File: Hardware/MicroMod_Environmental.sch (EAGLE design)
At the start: 36 parts, among them J1 MICROMOD_STANDARD, U1 SGP40, U2 EEPROM, U3 SHTC3, U4 3.3V, U5 STC31

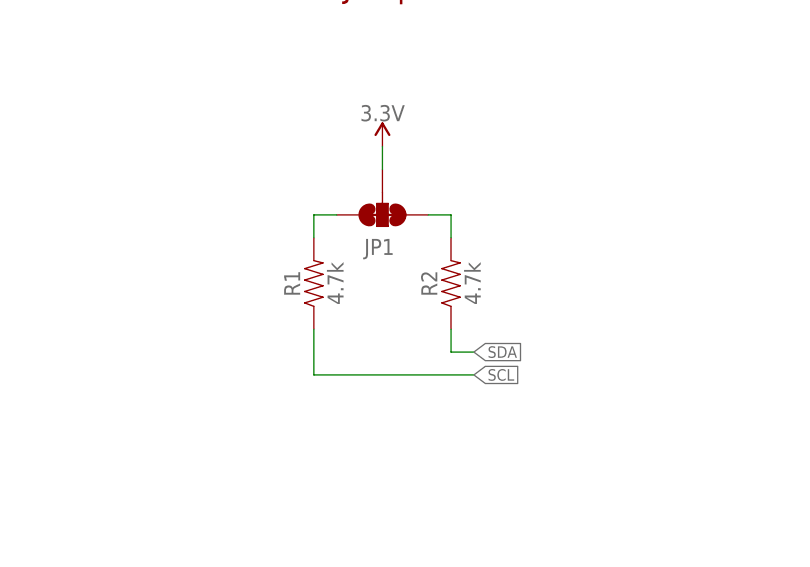
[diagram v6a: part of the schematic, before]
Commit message: Updates pull up resistors to 2.2k from 4.7k
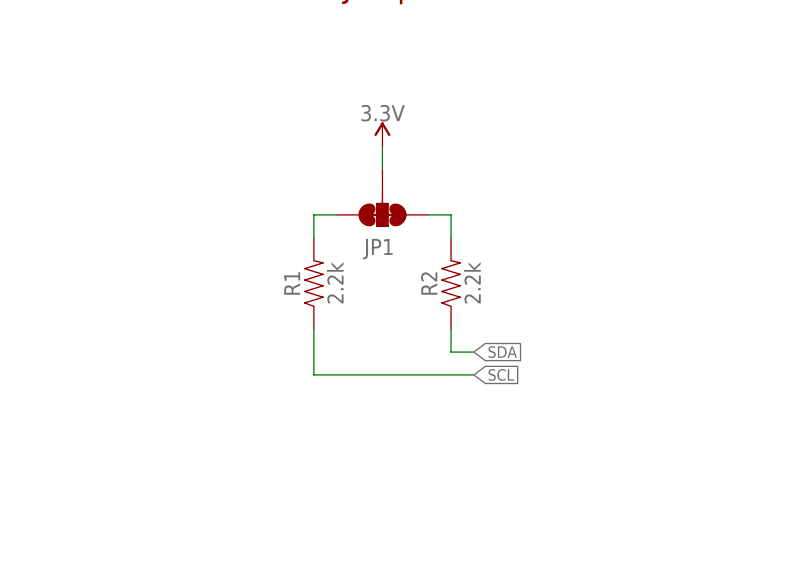
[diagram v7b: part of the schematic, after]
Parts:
- R1, R2: value 4.7k -> 2.2k; device SparkFun-Resistors:4.7KOHM-0603-1/10W-1% -> SparkFun-Resistors:2.2KOHM-0603-1/10W-1%
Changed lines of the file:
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@@
 <part name="FRAME1" library="SparkFun-Aesthetics" deviceset="FRAME-LEDGER" device=""/>
 <part name="J1" library="SparkFun-MicroMod-Function" deviceset="MICROMOD" device="_STANDARD"/>
-<part name="R1" library="SparkFun-Resistors" deviceset="4.7KOHM" device="-0603-1/10W-1%" value="4.7k"/>
-<part name="R2" library="SparkFun-Resistors" deviceset="4.7KOHM" device="-0603-1/10W-1%" value="4.7k"/>
+<part name="R1" library="SparkFun-Resistors" deviceset="2.2KOHM" device="-0603-1/10W-1%" value="2.2k"/>
+<part name="R2" library="SparkFun-Resistors" deviceset="2.2KOHM" device="-0603-1/10W-1%" value="2.2k"/>
 <part name="C5" library="SparkFun-Capacitors" deviceset="1.0UF" device="-0603-16V-10%" value="1.0uF"/>
 <part name="GND11" library="SparkFun-PowerSymbols" deviceset="GND" device=""/>
